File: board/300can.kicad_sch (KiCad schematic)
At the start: 46 parts, among them J101 Conn_01x10_Pin, U103 MCP2515-xSO, U104 SN65HVD230, U105 MCP2515-xSO, U106 SN65HVD230, U107 MCP2515-xSO, U108 SN65HVD230, U109 MCP2515-xSO, U110 SN65HVD230, U111 MCP2515-xSO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

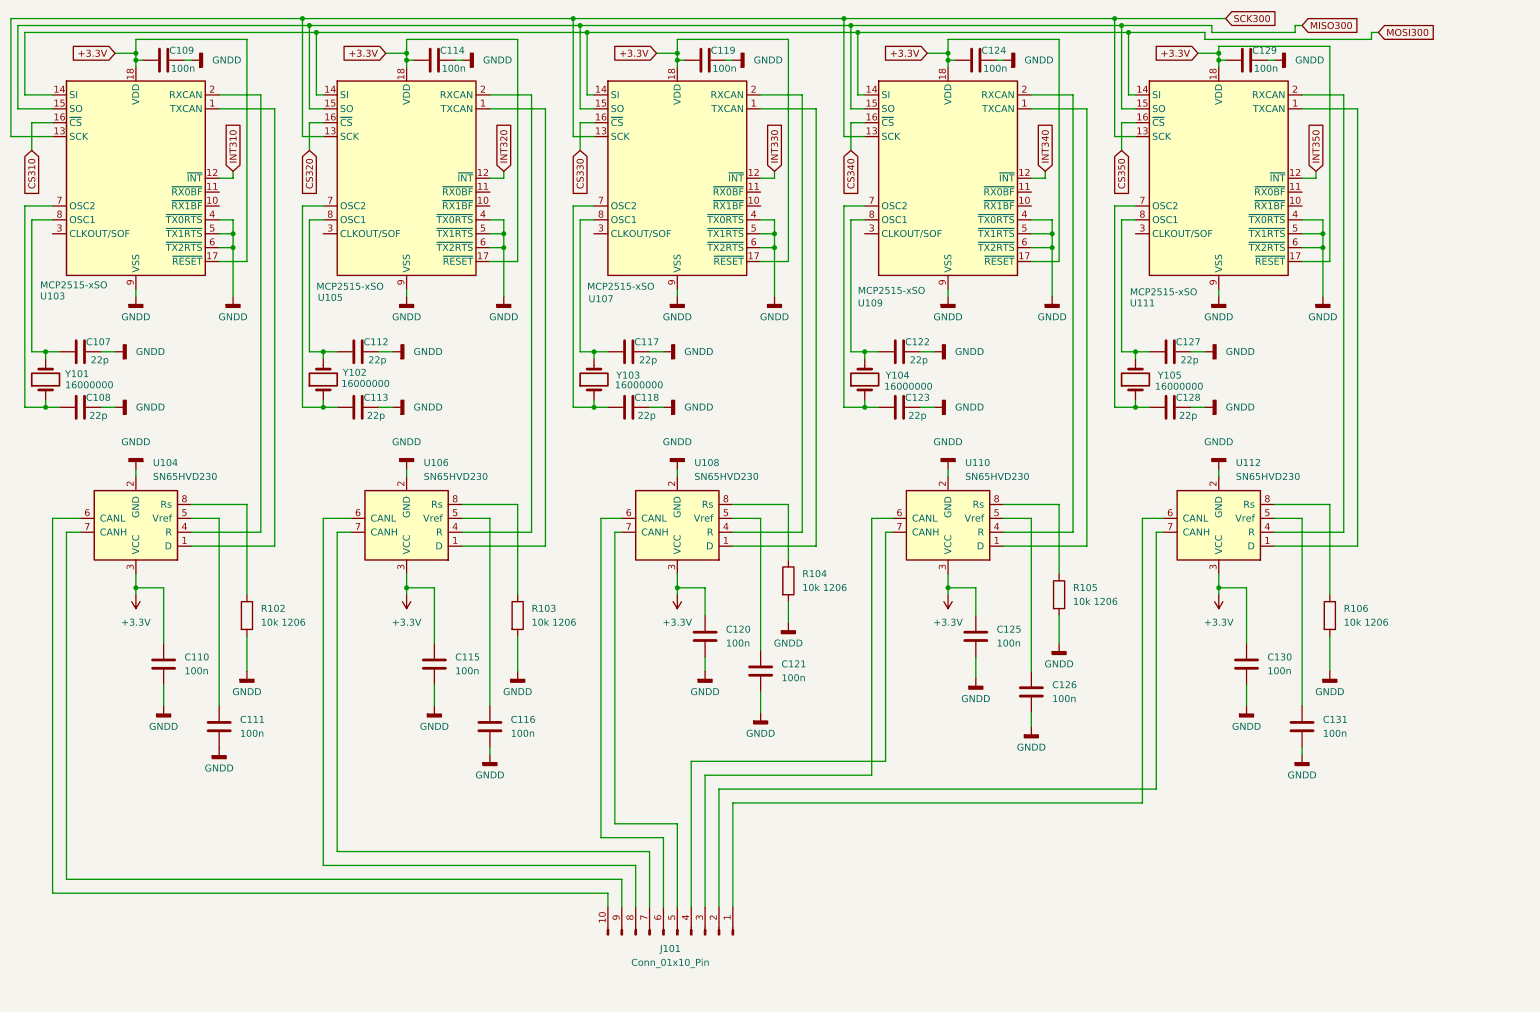
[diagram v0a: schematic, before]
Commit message: Added stl and skp files for 3D printing, changed ground planes and net names, exported schematics as pdf
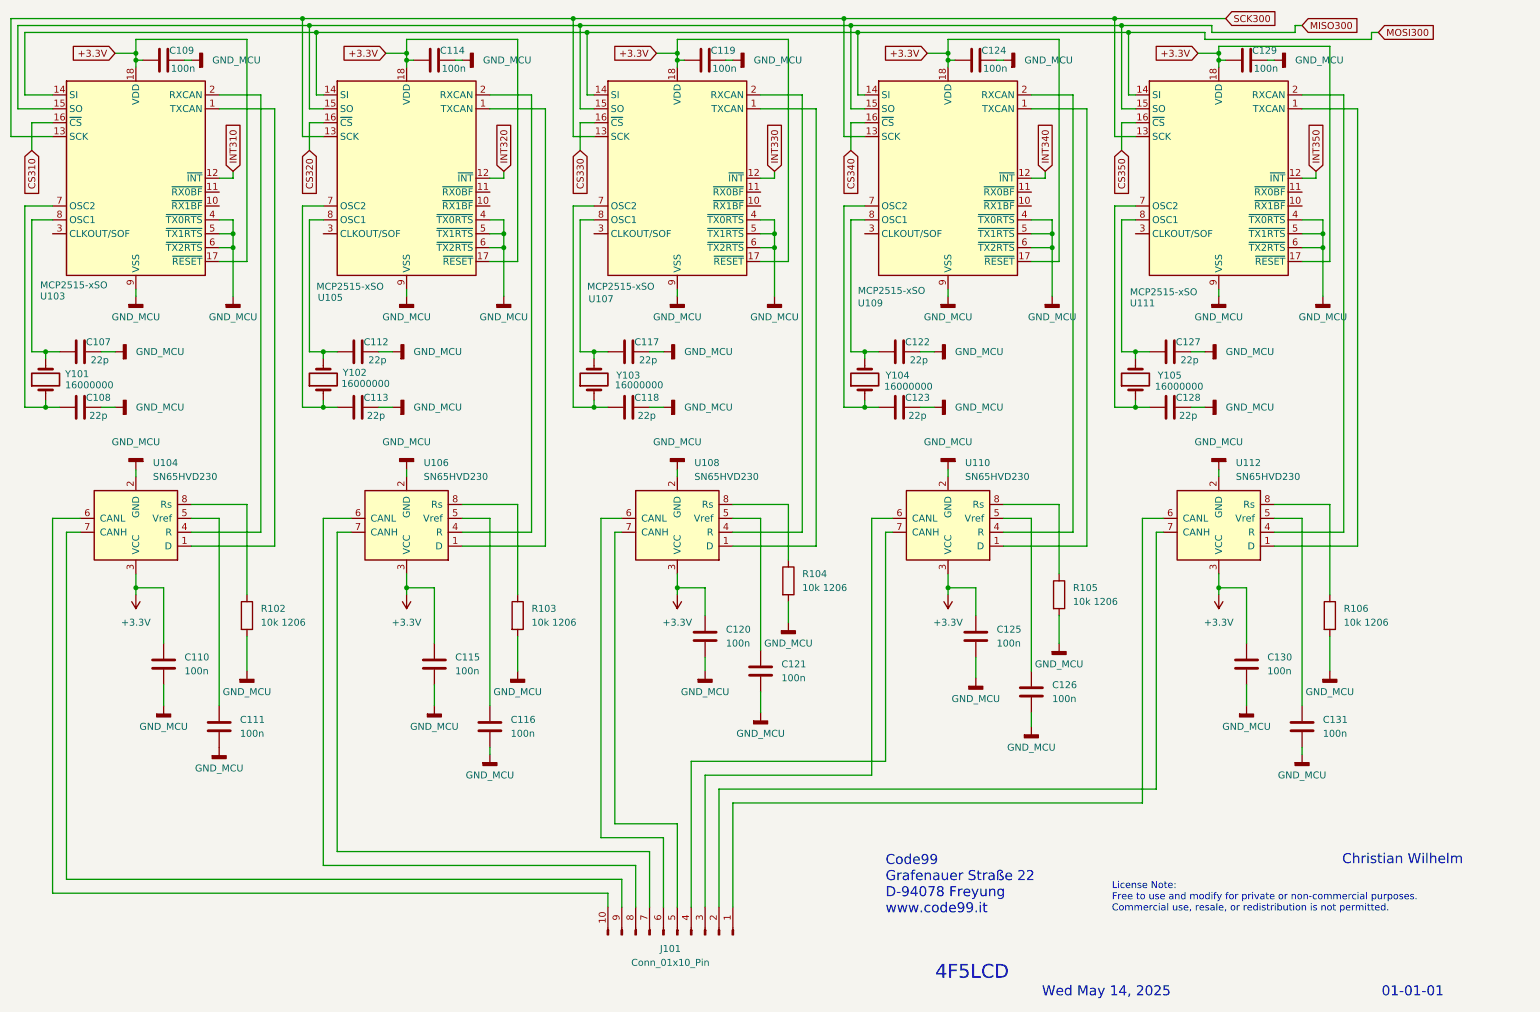
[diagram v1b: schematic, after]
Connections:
- net GNDD renamed GND_MCU
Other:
- note added: "01-01-01"
- note added: "4F5LCD"
- note added: "Christian Wilhelm"
- note added: "Code99 Grafenauer Straße 22 D-94078 Freyung www.code99.it"
- note added: "License Note: Free to use and modify for private or non-commercial purposes. Commercial use, resale, or redistribution is not permitted."
- note added: "Wed May 14, 2025"
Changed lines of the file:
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@@
 	(generator_version "9.0")
 	(paper "A4")
+	(text "Wed May 14, 2025"
+		(exclude_from_sim no)
+		(at 206.4143 193.346 0)
+		(effects
+			(font
+				(size 1.8288 1.8288)
+			)
+			(justify left)
+		)
+	)
+	(text "License Note:\nFree to use and modify for private or non-commercial purposes.\nCommercial use, resale, or redistribution is not permitted."
+		(exclude_from_sim no)
+		(at 219.202 176.022 0)
+		(effects
+			(font
+				(size 1.27 1.27)
+				(color 255 117 0 1)
+			)
+			(justify left)
+		)
+	)
+	(text "Code99\nGrafenauer Straße 22\nD-94078 Freyung\nwww.code99.it"
+		(exclude_from_sim no)
+		(at 177.8 173.736 0)
+		(effects
+			(font
+				(size 1.8288 1.8288)
+			)
+			(justify left)
+		)
+	)
+	(text "4F5LCD"
+		(exclude_from_sim no)
+		(at 186.8804 189.8105 0)
+		(effects
+			(font
+				(size 2.54 2.54)
+			)
+			(justify left)
+		)
+	)
+	(text "Christian Wilhelm"
+		(exclude_from_sim no)
+		(at 283.464 169.164 0)
+		(effects
+			(font
+				(size 1.8288 1.8288)
+			)
+			(justify right)
+		)
+	)
+	(text "01-01-01"
+		(exclude_from_sim no)
+		(at 268.5515 193.346 0)
+		(effects
+			(font
+				(size 1.8288 1.8288)
+			)
+			(justify left)
+		)
+	)
 	(junction
 		(at 71.12 15.24)
@@
 			)
 		)
-		(property "Value" "GNDD"
+		(property "Value" "GND_MCU"
 			(at 190.5 76.1999 90)
 			(effects
@@
 			)
 		)
-		(property "Value" "GNDD"
+		(property "Value" "GND_MCU"
 			(at 153.67 22.8599 90)
 			(effects
@@
 			)
 		)
-		(property "Value" "GNDD"
+		(property "Value" "GND_MCU"
 			(at 55.88 152.4 0)
 			(effects
@@
 			)
 		)
-		(property "Value" "GNDD"
+		(property "Value" "GND_MCU"
 			(at 254 153.67 0)
 			(effects
@@
 			)
 		)
-		(property "Value" "GNDD"
+		(property "Value" "GND_MCU"
 			(at 58.42 69.85 0)
 			(effects
@@
 			)
 		)
-		(property "Value" "GNDD"
+		(property "Value" "GND_MCU"
 			(at 40.64 92.71 0)
 			(effects
@@
 			)
 		)
-		(property "Value" "GNDD"
+		(property "Value" "GND_MCU"
 			(at 209.55 133.35 0)
 			(effects
@@
 			)
 		)
-		(property "Value" "GNDD"
+		(property "Value" "GND_MCU"
 			(at 140.97 76.1999 90)
 			(effects
@@
 			)
 		)
-		(property "Value" "GNDD"
+		(property "Value" "GND_MCU"
 			(at 238.76 69.85 0)
 			(effects
@@
 			)
 		)
-		(property "Value" "GNDD"
+		(property "Value" "GND_MCU"
 			(at 40.64 86.3599 90)
 			(effects
@@
 			)
 		)
-		(property "Value" "GNDD"
+		(property "Value" "GND_MCU"
 			(at 240.03 86.3599 90)
 			(effects
@@
 			)
 		)
-		(property "Value" "GNDD"
+		(property "Value" "GND_MCU"
 			(at 190.5 86.3599 90)
 			(effects
@@
 			)
 		)
-		(property "Value" "GNDD"
+		(property "Value" "GND_MCU"
 			(at 189.23 69.85 0)
 			(effects
@@
 			)
 		)
-		(property "Value" "GNDD"
+		(property "Value" "GND_MCU"
 			(at 40.64 69.85 0)
 			(effects
@@
 			)
 		)
-		(property "Value" "GNDD"
+		(property "Value" "GND_MCU"
 			(at 45.72 144.78 0)
 			(effects
@@
 			)
 		)
-		(property "Value" "GNDD"
+		(property "Value" "GND_MCU"
 			(at 110.49 138.43 0)
 			(effects
@@
 			)
 		)
-		(property "Value" "GNDD"
+		(property "Value" "GND_MCU"
 			(at 157.48 69.85 0)
 			(effects
@@
 			)
 		)
-		(property "Value" "GNDD"
+		(property "Value" "GND_MCU"
 			(at 90.17 92.71 0)
 			(effects
@@
 			)
 		)
-		(property "Value" "GNDD"
+		(property "Value" "GND_MCU"
 			(at 104.14 22.8599 90)
 			(effects
@@
 			)
 		)
-		(property "Value" "GNDD"
+		(property "Value" "GND_MCU"
 			(at 91.44 86.3599 90)
 			(effects
@@
 			)
 		)
-		(property "Value" "GNDD"
+		(property "Value" "GND_MCU"
 			(at 189.23 92.71 0)
 			(effects
@@
 			)
 		)
-		(property "Value" "GNDD"
+		(property "Value" "GND_MCU"
 			(at 105.41 153.67 0)
 			(effects
@@
 			)
 		)
-		(property "Value" "GNDD"
+		(property "Value" "GND_MCU"
 			(at 257.81 69.85 0)
 			(effects
@@
 			)
 		)
-		(property "Value" "GNDD"
+		(property "Value" "GND_MCU"
 			(at 144.78 138.43 0)
 			(effects
@@
 			)
 		)
-		(property "Value" "GNDD"
+		(property "Value" "GND_MCU"
 			(at 204.47 148.59 0)
 			(effects
@@
 			)
 		)
-		(property "Value" "GNDD"
+		(property "Value" "GND_MCU"
 			(at 60.96 138.43 0)
 			(effects
@@
 			)
 		)
-		(property "Value" "GNDD"
+		(property "Value" "GND_MCU"
 			(at 240.03 76.1999 90)
 			(effects
@@
 			)
 		)
-		(property "Value" "GNDD"
+		(property "Value" "GND_MCU"
 			(at 95.25 144.78 0)
 			(effects
@@
 			)
 		)
-		(property "Value" "GNDD"
+		(property "Value" "GND_MCU"
 			(at 139.7 69.85 0)
 			(effects
@@
 			)
 		)
-		(property "Value" "GNDD"
+		(property "Value" "GND_MCU"
 			(at 40.64 76.1999 90)
 			(effects
@@
 			)
 		)
-		(property "Value" "GNDD"
+		(property "Value" "GND_MCU"
 			(at 107.95 69.85 0)
 			(effects
@@
 			)
 		)
-		(property "Value" "GNDD"
+		(property "Value" "GND_MCU"
 			(at 252.73 22.8599 90)
 			(effects
@@
 			)
 		)
-		(property "Value" "GNDD"
+		(property "Value" "GND_MCU"
 			(at 243.84 144.78 0)
 			(effects
@@
 			)
 		)
-		(property "Value" "GNDD"
+		(property "Value" "GND_MCU"
 			(at 259.08 138.43 0)
 			(effects
@@
 			)
 		)
-		(property "Value" "GNDD"
+		(property "Value" "GND_MCU"
 			(at 54.61 22.8599 90)
 			(effects
@@
 			)
 		)
-		(property "Value" "GNDD"
+		(property "Value" "GND_MCU"
 			(at 194.31 139.7 0)
 			(effects
@@
 			)
 		)
-		(property "Value" "GNDD"
+		(property "Value" "GND_MCU"
 			(at 91.44 76.1999 90)
 			(effects
@@
 			)
 		)
-		(property "Value" "GNDD"
+		(property "Value" "GND_MCU"
 			(at 140.97 86.3599 90)
 			(effects
@@
 			)
 		)
-		(property "Value" "GNDD"
+		(property "Value" "GND_MCU"
 			(at 160.02 129.54 0)
 			(effects
@@
 			)
 		)
-		(property "Value" "GNDD"
+		(property "Value" "GND_MCU"
 			(at 208.28 69.85 0)
 			(effects
@@
 			)
 		)
-		(property "Value" "GNDD"
+		(property "Value" "GND_MCU"
 			(at 139.7 92.71 0)
 			(effects
@@
 			)
 		)
-		(property "Value" "GNDD"
+		(property "Value" "GND_MCU"
 			(at 238.76 92.71 0)
 			(effects
@@
 			)
 		)
-		(property "Value" "GNDD"
+		(property "Value" "GND_MCU"
 			(at 203.2 22.8599 90)
 			(effects
@@
 			)
 		)
-		(property "Value" "GNDD"
+		(property "Value" "GND_MCU"
 			(at 154.94 146.05 0)
 			(effects
@@
 			)
 		)
-		(property "Value" "GNDD"
+		(property "Value" "GND_MCU"
 			(at 90.17 69.85 0)
 			(effects
